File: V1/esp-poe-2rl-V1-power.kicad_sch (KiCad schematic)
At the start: 39 parts, among them Q1 WPM2015-3/TR, Q2 LMUN2211LT1G, U1 SY8089A1AAC, U2 TX4138, U6 TPS2376

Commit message: Dev
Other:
- title: ESP 16x 24VDC Input 16x 24VDC Output Module -> ESP 2x Relay Output Module with PoE
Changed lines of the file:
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@@
   (paper "A4")
   (title_block
-    (title "ESP 16x 24VDC Input 16x 24VDC Output Module")
-    (date "2023-05-05")
-    (rev "V2")
+    (title "ESP 2x Relay Output Module with PoE")
+    (date "2023-08-02")
+    (rev "V1")
   )
   (junction (at 180.34 46.99) (diameter 0) (color 0 0 0 0)

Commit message: Searching for the right connector...
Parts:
- removed U6: TPS2376, Package_SO:SOIC-8-1EP_3.9x4.9mm_P1.27mm_EP2.95x4.9mm_Mask2.71x3.4mm_ThermalVias, symbol Tales:TPS2376
- R1: value 5,6k/0,1W/0603 -> 820R/62,5mW/0402; footprint Tales:R_0603_1608Metric -> Tales:R_0402_1005Metric; Case 0603/1608 -> 0402/1005; LCSC Part # C23189 -> C423266; Mfr PN 0603WAF5601T5E -> 0402WGD8200TCE; Vendor PN C23189 -> C423266
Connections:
- net +24V: no longer R1.1
- net +5V: now also R1.1
- net GND: no longer J?.2 (Pin_2)
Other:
- note added: "5VDC"
- note added: "R_{1}"
- note added: "R_{1} = (V_{OUT} - 0,6V) * R_{2} / 0,6V V_{OUT} = (0,6 * R_{1} / R_{2}) + 0,6 V_{OUT} = (0,6 * 100k/22,1k) +0,6 V_{OUT} = 3,31V"
- note added: "R_{2}"
- note removed: "24VDC"
- note removed: "R1"
- note removed: "R2"
- note removed: "RH"
- note removed: "RL"
- note removed: "R_{H} = (V_{OUT} - 0,6V) * R_{L} / 0,6V V_{OUT} = (0,6 * R_{H} / R_{L}) + 0,6 V_{OUT} = (0,6 * 100k/22,1k) +0,6 V_{OUT} = 3,31V"
- moved on the sheet: C1, C10, C2, C3, C39, C4, C40, C5, C7, C8, D1, D2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

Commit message: Working on PoE frontend.
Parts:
- removed C4: 0,1uF/50V/0805, Tales:C_0805_2012Metric, symbol Device:C_Small
- added C23: 100nF/100V, Tales:C_1206_3216Metric, symbol Device:C_Small
- added D7: SMAJ58A, Tales:D_SMA, symbol Device:D_Zener_Small
- added R13, R14, R34: R_US, symbol Device:R_US
- added R31: 29,9k/62,5mW, Tales:R_0402_1005Metric, symbol Device:R_US
- added R32: 4,42k/62,5mW, Tales:R_0402_1005Metric, symbol Device:R_US
- added R33: 180k/62,5mW, Tales:R_0402_1005Metric, symbol Device:R_US
- added U6: TPS2376D, Package_SO:SOIC-8-1EP_3.9x4.9mm_P1.27mm_EP2.95x4.9mm_Mask2.71x3.4mm_ThermalVias, symbol Tales:TPS2376
- C1, C5: value 10uF/50V/1206 -> 10uF/50V
- C10: value 470uF/16V/10x10 -> 470uF/16V
- C2: value 47uF/35V/6,3x5,4 -> 15uF/100V; footprint Tales:CP_Elec_6.3x5.4 -> (none); Case 6,3x5,4 -> 6,3x11; LCSC Part # C263963 -> C???; Mfr Semtech -> (none); Mfr PN CK1V470MCRE54 -> (none); Vendor PN C263963 -> C???
- C3: value 22pF/50V/0603 -> 22pF/50V
- C39: value 1uF/50V/0603 -> 1uF/50V
- C40: value 0,1uF/50V/0402 -> 0,1uF/50V
- C6, C9: value 10uF/10V/0603 -> 10uF/10V
- C7: value 0,1uF/50V/0805 -> 0,1uF/50V
- C8: value 12pF/50V/0603 -> 12pF/50V
- D1: value SM4007PL/SOD-123 -> SM4007PL
- D2: value GREEN/0603 -> GREEN
- L1: value 2,2uH 1,5A -> 2,2uH/1,5A
- L2: value 33uH 2,1A -> 33uH/2,1A
- L3: value 2A 600R -> 2A/600R
- R1: value 820R/62,5mW/0402 -> 820R/62,5mW
- R131, R132: value 5k1/62,5mW/0402 -> 5k1/62,5mW
- R2: value 100k/0,125W/0805 -> 100k/0,125W
- R3: value 22,1k/0,125W/0805 -> 22,1k/0,125W
- R4: value 30mR/0,250W/0805 -> 30mR/0,250W; Technology (none) -> 1%
- R5: value 5R1/0,125W/0805 -> 5R1/0,125W; Technology (none) -> 1%
- R6: value 10k/62,5mW/0402 -> 10k/62,5mW
- R7: value 1k/62,5mW/0402 -> 1k/62,5mW
- R8: value 300k/0,125W/0805 -> 300k/0,125W; Technology (none) -> 1%
- R9: value 52,3k/0,125W/0805 -> 52,3k/0,125W; Technology (none) -> 1%
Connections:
- net +5V: now also F1.1; no longer F1.2
- net GND: now also R34.2, U6.5 (RTN)
- net at D3.1 (K): now also F1.2; no longer F1.1
- net at D1.2 (A): no longer J?.1 (Pin_1)
- net PoE+: now reaches R4.1, U2.3 (VIN)
- net PoE+: now also C2.1, C23.1, D7.1 (K), R13.1, R31.1, R34.1, U6.8 (VDD)
- net at U2.6 (EN): now also U6.6 (PG)
- net +24V: no longer names the net of D1.1 (K)
- net +24V: no longer C2.1
- new net: R13.2, R14.1, U6.7 (UVLO)
- new net: R33.1, U6.1 (ILIM)
- new net: R32.1, U6.2 (CLASS)
- new net: R31.2, U6.3 (DET)
- new net PoE-: C23.2, D7.2 (A), R14.2, R32.2, R33.2, U6.4 (VSS)
- no-connect marks 4 -> 3
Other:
- moved on the sheet: C1, C10, C2, C3, C39, C40, C5, C6, C7, C8, D1, D2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

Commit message: Development
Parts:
- removed D1: SM4007PL, Tales:D_SOD-123, symbol Device:D_Small
- removed J?: VIN, Tales:TerminalBlock_Phoenix_MKDS-3-2-5.08_1x02_P5.08mm_Horizontal, symbol Connector_Generic:Conn_01x02
- C2: footprint (none) -> Capacitor_SMD:CP_Elec_8x6.2; Case 6,3x11 -> 8x6,2; LCSC Part # C??? -> C487174; Mfr (none) -> Ymin; Mfr PN (none) -> VMMD0622A150MV; Vendor PN C??? -> C487174
- R13: value R_US -> 412k/62,5mW; footprint (none) -> Tales:R_0402_1005Metric; Case (none) -> 0402/1005; JLCPCB BOM (none) -> 1; LCSC Part # (none) -> C187991; Mfr (none) -> TA-I Tech; Mfr PN (none) -> RM04FTN4123; Technology (none) -> 1%; Vendor (none) -> JLCPCB; Vendor PN (none) -> C187991
- R14: value R_US -> 31.6k/62,5mW; footprint (none) -> Tales:R_0402_1005Metric; Case (none) -> 0402/1005; JLCPCB BOM (none) -> 1; LCSC Part # (none) -> C100371; Mfr (none) -> LIZ Elec; Mfr PN (none) -> CR0402FF3162G; Technology (none) -> 1%; Vendor (none) -> JLCPCB; Vendor PN (none) -> C100371
- R31: value 29,9k/62,5mW -> 26,7k/62,5mW; LCSC Part # C100335 -> C304992; Mfr LIZ Elec -> Ralec; Mfr PN CR0402FF2492G -> RTT022672DTH; Technology 1% -> 0,5%; Vendor PN C100335 -> C304992
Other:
- note added: "R_{2} = R_{1}/(V_{OUT} / 0,805 - 1) V_{OUT} = (R_{1} / R_{2}) + 1) * 0,805 V_{OUT} = (300k / 52,3k + 1) * 0,805 V_{OUT} = 5,42V VOLTAGE DROP AT DIODE SS34 @2A = 0,4V 5V MAIN BUS @2A = 5,02V"
- note added: "R_{CLASS}"
- note added: "R_{CLASS} = 4420R 1% CLASS 0 0.44 - 12,95W"
- note added: "R_{DET}"
- note added: "USB 2.0 -> 5V 500mA USB 3.0 -> 5V 900mA VOLTAGE DROP AT DIODE B5819W @500mA = 0,4V 5V USB BUS @500mA = 4,6V"
- note added: "VOLTAGE AT THE TAP OF THE DIVIDER R_{1}/R_{2} (PIN UVLO) MUST BE 2,5V WHEN VDD IS AT THE DESIRED TURN ON VOLTAGE. THE TOTAL RESISTANCE OF THE VOLTAGE DIVIDER WILL APPEAR IN PARALLEL WITH R_{DET} TO FORM THE EQUIVALENT RESISTANCE AT PIN DET."
- note removed: "5VDC"
- note removed: "R_{2} = R_{1}/(V_{OUT} / 0,805 - 1) V_{OUT} = (R_{1} / R_{2}) + 1) * 0,805 V_{OUT} = (300k / 52,3k + 1) * 0,805 V_{OUT} = 5,42V"
- moved on the sheet: C1, C10, C2, C23, C3, C39, C40, C5, C6, C7, C8, C9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

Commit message: Development continues!
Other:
- note added: "V_{TAP}"
- note added: "V_{TAP} MUST BE 2.5V WHEN VDD IS AT THE DESIRED TURN ON VOLTAGE. V_{TAP} = V_{DD} * R_{2} / (R_{1}+R_{2}) 2.5 = V_{DD} * 31.6 / 443.6 V_{DD} = 35.1V -> OK THE TOTAL RESISTANCE OF THE VOLTAGE DIVIDER (R_{1} + R_{2}) WILL APPEAR IN PARALLEL WITH R_{DET} TO FORM THE EQUIVALENT RESISTANCE AT PIN DET. R_{EQUIV} = (R_{1} + R_{2}) // R_{DET} R_{EQUIV} = 443.6 // 26.7 R_{EQUIV} = 25.184k -> OK"
- note removed: "VOLTAGE AT THE TAP OF THE DIVIDER R_{1}/R_{2} (PIN UVLO) MUST BE 2,5V WHEN VDD IS AT THE DESIRED TURN ON VOLTAGE. THE TOTAL RESISTANCE OF THE VOLTAGE DIVIDER WILL APPEAR IN PARALLEL WITH R_{DET} TO FORM THE EQUIVALENT RESISTANCE AT PIN DET."
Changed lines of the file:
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@@
     (effects (font (size 1.5 1.5)) (justify left bottom))
   )
-  (text "R_{CLASS} = 4420R 1%\nCLASS 0\n0.44 - 12,95W" (at 105.41 78.74 0)
+  (text "R_{CLASS} = 4420R 1%\nCLASS 0\n0.44 - 12,95W" (at 92.71 78.74 0)
     (effects (font (size 1.5 1.5)) (justify left bottom))
   )
-  (text "VOLTAGE AT THE TAP OF THE DIVIDER R_{1}/R_{2} (PIN UVLO)\nMUST BE 2,5V WHEN VDD IS AT THE DESIRED TURN ON VOLTAGE.\n\nTHE TOTAL RESISTANCE OF THE VOLTAGE DIVIDER WILL APPEAR\nIN PARALLEL WITH R_{DET} TO FORM THE EQUIVALENT RESISTANCE AT\nPIN DET."
-    (at 26.67 86.36 0)
+  (text "V_{TAP} MUST BE 2.5V WHEN VDD IS AT THE\nDESIRED TURN ON VOLTAGE.\n\nV_{TAP} = V_{DD} * R_{2} / (R_{1}+R_{2})\n2.5 = V_{DD} * 31.6 / 443.6\nV_{DD} = 35.1V -> OK\n\nTHE TOTAL RESISTANCE OF THE VOLTAGE DIVIDER\n(R_{1} + R_{2}) WILL APPEAR IN PARALLEL WITH\nR_{DET} TO FORM THE EQUIVALENT RESISTANCE AT\nPIN DET.\n\nR_{EQUIV} = (R_{1} + R_{2}) // R_{DET}\nR_{EQUIV} = 443.6 // 26.7\nR_{EQUIV} = 25.184k -> OK"
+    (at 33.02 107.95 0)
     (effects (font (size 1.5 1.5)) (justify left bottom))
   )
@@
     (effects (font (size 1.5 1.5)) (justify left bottom))
   )
+  (text "V_{TAP}" (at 59.69 49.53 0)
+    (effects (font (size 1.5 1.5)) (justify left bottom))
+  )

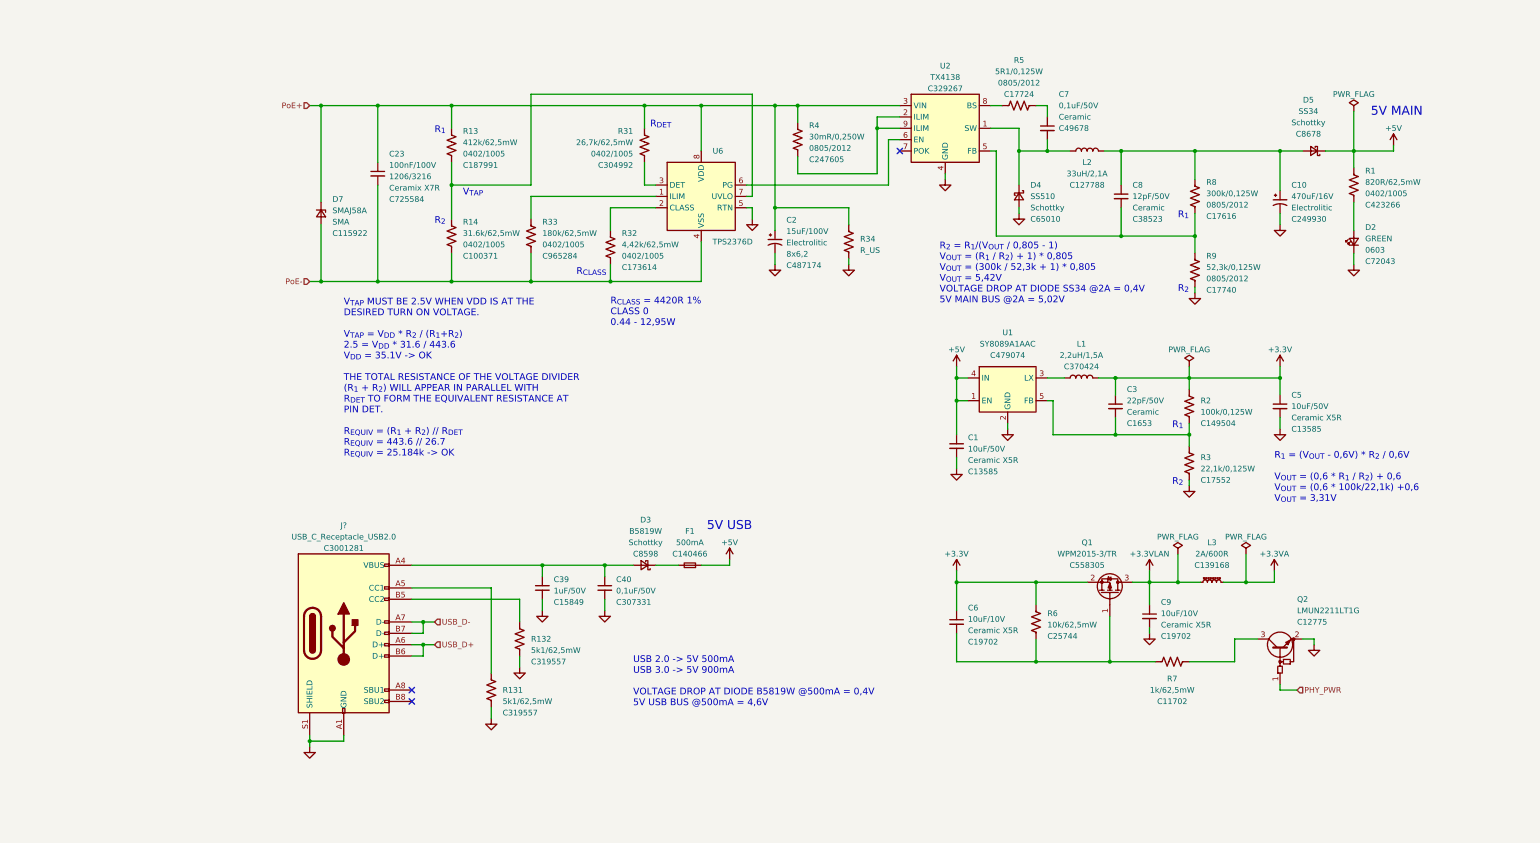
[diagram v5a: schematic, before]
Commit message: Topology ok, checking components values
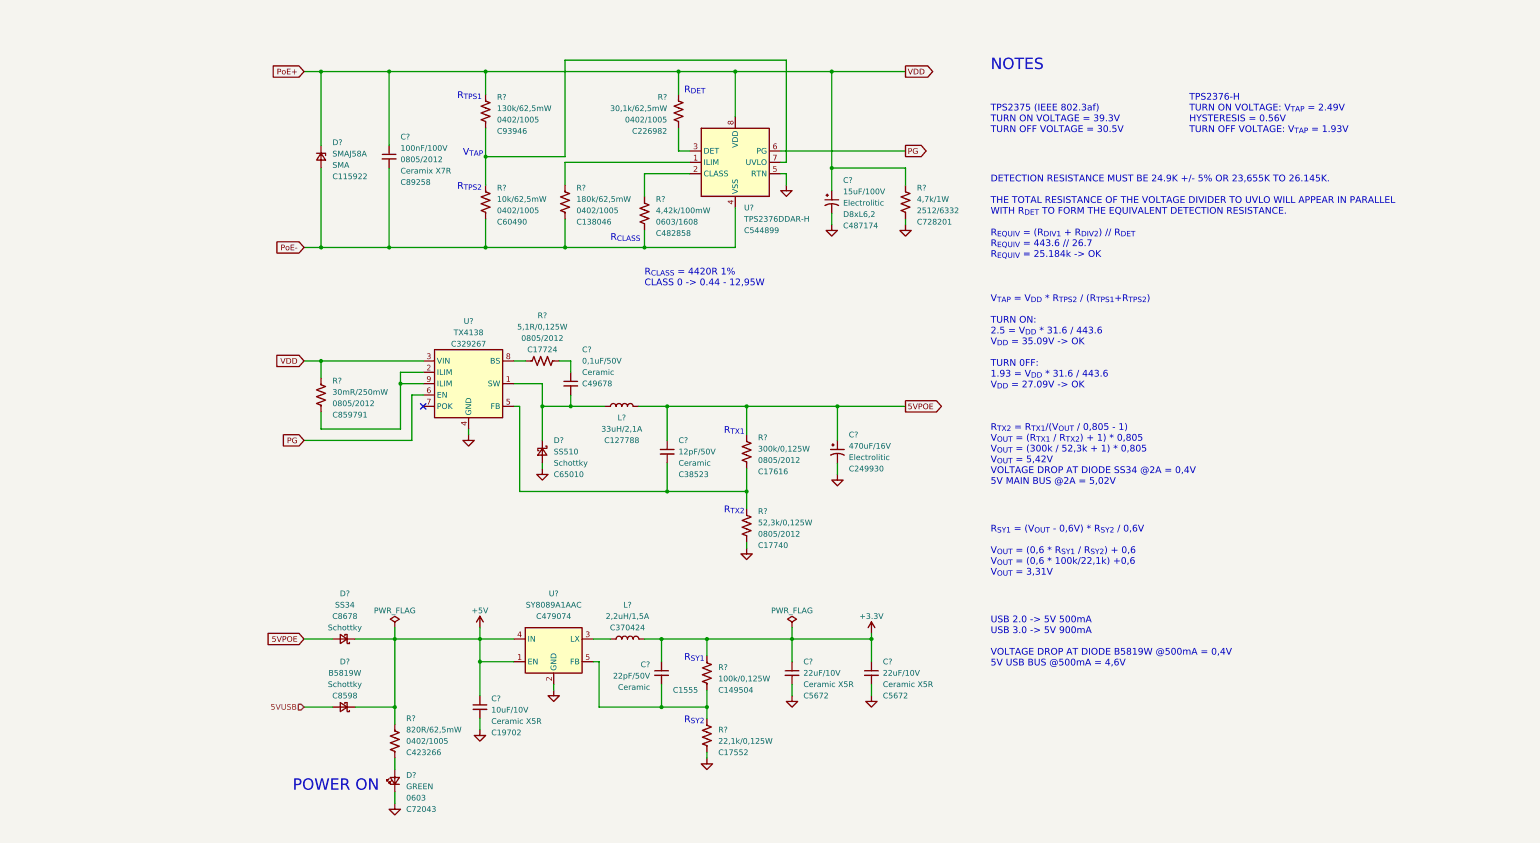
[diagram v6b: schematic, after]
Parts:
- removed C1, C5: 10uF/50V, Tales:C_1206_3216Metric, symbol Device:C_Small
- removed C10: 470uF/16V, Tales:CP_Elec_10x10, symbol Device:C_Polarized_Small_US
- removed C2: 15uF/100V, Capacitor_SMD:CP_Elec_8x6.2, symbol Device:C_Polarized_Small_US
- removed C23: 100nF/100V, Tales:C_1206_3216Metric, symbol Device:C_Small
- removed C3: 22pF/50V, Tales:C_0603_1608Metric, symbol Device:C_Small
- removed C39: 1uF/50V, Tales:C_0603_1608Metric, symbol Device:C_Small
- removed C40: 0,1uF/50V, Tales:C_0402_1005Metric, symbol Device:C_Small
- removed C6, C9: 10uF/10V, Tales:C_0603_1608Metric, symbol Device:C_Small
- removed C7: 0,1uF/50V, Tales:C_0805_2012Metric, symbol Device:C_Small
- removed C8: 12pF/50V, Tales:C_0603_1608Metric, symbol Device:C_Small
- removed D2: GREEN, Tales:LED_0603_1608Metric, symbol Device:LED_Small
- removed D3: B5819W, Tales:D_SOD-123, symbol Device:D_Schottky_Small
- removed D4: SS510, Tales:D_SMA, symbol Device:D_Schottky_Small
- removed D5: SS34, Tales:D_SMA, symbol Device:D_Schottky_Small
- removed D7: SMAJ58A, Tales:D_SMA, symbol Device:D_Zener_Small
- removed F1: 500mA, Fuse:Fuse_1206_3216Metric, symbol Device:Fuse_Small
- removed J?: USB_C_Receptacle_USB2.0, Tales:USB_C_Receptacle_JAE_DX07S024WJ1R350, symbol Connector:USB_C_Receptacle_USB2.0
- removed L1: 2,2uH/1,5A, Tales:L_3x3_H1.5, symbol Device:L
- removed L2: 33uH/2,1A, Tales:L_12x12mm_H6mm, symbol Device:L
- removed L3: 2A/600R, Inductor_SMD:L_0805_2012Metric, symbol Device:L_Ferrite_Small
- removed Q1: WPM2015-3/TR, Tales:SOT-23, symbol Device:Q_PMOS_GSD
- removed Q2: LMUN2211LT1G, Tales:SOT-23, symbol Device:Q_NPN_BEC_BRT
- removed R1: 820R/62,5mW, Tales:R_0402_1005Metric, symbol Device:R_US
- removed R13: 412k/62,5mW, Tales:R_0402_1005Metric, symbol Device:R_US
- removed R131, R132: 5k1/62,5mW, Tales:R_0402_1005Metric, symbol Device:R_US
- removed R14: 31.6k/62,5mW, Tales:R_0402_1005Metric, symbol Device:R_US
- removed R2: 100k/0,125W, Tales:R_0805_2012Metric, symbol Device:R_US
- removed R3: 22,1k/0,125W, Tales:R_0805_2012Metric, symbol Device:R_US
- removed R31: 26,7k/62,5mW, Tales:R_0402_1005Metric, symbol Device:R_US
- removed R32: 4,42k/62,5mW, Tales:R_0402_1005Metric, symbol Device:R_US
- removed R33: 180k/62,5mW, Tales:R_0402_1005Metric, symbol Device:R_US
- removed R34: R_US, symbol Device:R_US
- removed R4: 30mR/0,250W, Tales:R_0805_2012Metric, symbol Device:R_US
- removed R5: 5R1/0,125W, Tales:R_0805_2012Metric, symbol Device:R_US
- removed R6: 10k/62,5mW, Tales:R_0402_1005Metric, symbol Device:R_US
- removed R7: 1k/62,5mW, Tales:R_0402_1005Metric, symbol Device:R_US
- removed R8: 300k/0,125W, Tales:R_0805_2012Metric, symbol Device:R_US
- removed R9: 52,3k/0,125W, Tales:R_0805_2012Metric, symbol Device:R_US
- removed U1: SY8089A1AAC, Tales:TSOT-23-5, symbol Tales:SY8089AAAC
- removed U2: TX4138, Tales:SOIC-8-1EP_3.9x4.9mm_P1.27mm_EP2.29x3mm_ThermalVias, symbol Tales:TX4138
- removed U6: TPS2376D, Package_SO:SOIC-8-1EP_3.9x4.9mm_P1.27mm_EP2.95x4.9mm_Mask2.71x3.4mm_ThermalVias, symbol Tales:TPS2376
- added C? (x2): 22uF/10V, Tales:C_1206_3216Metric, symbol Device:C_Small
- added C?: 0,1uF/50V, Tales:C_0805_2012Metric, symbol Device:C_Small
- added C?: 100nF/100V, Tales:C_0805_2012Metric, symbol Device:C_Small
- added C?: 22pF/50V, Tales:C_0402_1005Metric, symbol Device:C_Small
- added C?: 15uF/100V, Capacitor_SMD:CP_Elec_8x6.2, symbol Device:C_Polarized_Small_US
- added C?: 12pF/50V, Tales:C_0603_1608Metric, symbol Device:C_Small
- added C?: 470uF/16V, Tales:CP_Elec_10x10, symbol Device:C_Polarized_Small_US
- added C?: 10uF/10V, Tales:C_0603_1608Metric, symbol Device:C_Small
- added D?: SS34, Tales:D_SMA, symbol Device:D_Schottky_Small
- added D?: SS510, Tales:D_SMA, symbol Device:D_Schottky_Small
- added D?: SMAJ58A, Tales:D_SMA, symbol Device:D_Zener_Small
- added D?: GREEN, Tales:LED_0603_1608Metric, symbol Device:LED_Small
- added D?: B5819W, Tales:D_SOD-123, symbol Device:D_Schottky_Small
- added L?: 2,2uH/1,5A, Tales:L_3x3_H1.5, symbol Device:L
- added L?: 33uH/2,1A, Tales:L_12x12mm_H6mm, symbol Device:L
- added R?: 5,1R/0,125W, Tales:R_0805_2012Metric, symbol Device:R_US
- added R?: 52,3k/0,125W, Tales:R_0805_2012Metric, symbol Device:R_US
- added R?: 130k/62,5mW, Tales:R_0402_1005Metric, symbol Device:R_US
- added R?: 4,7k/1W, Tales:R_2512_6332Metric, symbol Device:R_US
- added R?: 180k/62,5mW, Tales:R_0402_1005Metric, symbol Device:R_US
- added R?: 30,1k/62,5mW, Tales:R_0402_1005Metric, symbol Device:R_US
- added R?: 300k/0,125W, Tales:R_0805_2012Metric, symbol Device:R_US
- added R?: 100k/0,125W, Tales:R_0805_2012Metric, symbol Device:R_US
- added R?: 4,42k/100mW, Tales:R_0603_1608Metric, symbol Device:R_US
- added R?: 30mR/250mW, Tales:R_0805_2012Metric, symbol Device:R_US
- added R?: 10k/62,5mW, Tales:R_0402_1005Metric, symbol Device:R_US
- added R?: 820R/62,5mW, Tales:R_0402_1005Metric, symbol Device:R_US
- added R?: 22,1k/0,125W, Tales:R_0805_2012Metric, symbol Device:R_US
- added U?: TPS2376DDAR-H, Package_SO:SOIC-8-1EP_3.9x4.9mm_P1.27mm_EP2.95x4.9mm_Mask2.71x3.4mm_ThermalVias, symbol Tales:TPS2376
- added U?: TX4138, Tales:SOIC-8-1EP_3.9x4.9mm_P1.27mm_EP2.29x3mm_ThermalVias, symbol Tales:TX4138
- added U?: SY8089A1AAC, Tales:TSOT-23-5, symbol Tales:SY8089AAAC
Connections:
- net +3.3V: now also C?.1, C?.1, C?.1, L?.2, R?.1
- net +5V: now also C?.1, D?.1 (K), D?.1 (K), R?.1, U?.1 (EN), U?.4 (IN)
- net GND: now also C?.2, C?.2, C?.2, C?.2, C?.2, D?.1 (K), D?.2 (A), R?.2, R?.2, R?.2, U?.2 (GND), U?.4 (GND), U?.5 (RTN)
- net PoE+: now also C?.1, C?.1, D?.1 (K), R?.1, R?.1, R?.1, R?.1, U?.3 (VIN), U?.8 (VDD)
- net PoE-: now also C?.2, D?.2 (A), R?.2, R?.2, R?.2, U?.4 (VSS)
- new net: C?.1, R?.1
- new net: R?.2, U?.8 (BS)
- new net: C?.2, D?.1 (K), L?.1, U?.1 (SW)
- new net: C?.2, R?.1, R?.2, U?.5 (FB) (x2)
- new net: L?.1, U?.3 (LX)
- new net: R?.1, R?.2, U?.7 (UVLO)
- new net: R?.1, U?.1 (ILIM)
- new net: R?.1, U?.2 (CLASS)
- new net: R?.2, U?.3 (DET)
- new net: R?.2, U?.2 (ILIM), U?.9 (ILIM)
- new net: D?.2 (A), R?.2
- new net 5VPOE: C?.1, C?.1, D?.2 (A), L?.2, R?.1
- new net 5VUSB: D?.2 (A)
- new net PG: U?.6 (EN), U?.6 (PG)
- no-connect marks 3 -> 1
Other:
- note added: "DETECTION RESISTANCE MUST BE 24.9K +/- 5% OR 23,655K TO 26.145K. THE TOTAL RESISTANCE OF THE VOLTAGE DIVIDER TO UVLO WILL APPEAR IN PARALLEL WITH R_{DET} TO FORM THE EQUIVALENT DETECTION RESISTANCE. R_{EQUIV} = (R_{DIV1} + R_{DIV2}) // R_{DET} R_{EQUIV} = 443.6 // 26.7 R_{EQUIV} = 25.184k -> OK"
- note added: "NOTES"
- note added: "POWER ON"
- note added: "R_{CLASS} = 4420R 1% CLASS 0 -> 0.44 - 12,95W"
- note added: "R_{SY1}"
- note added: "R_{SY1} = (V_{OUT} - 0,6V) * R_{SY2} / 0,6V V_{OUT} = (0,6 * R_{SY1} / R_{SY2}) + 0,6 V_{OUT} = (0,6 * 100k/22,1k) +0,6 V_{OUT} = 3,31V"
- note added: "R_{SY2}"
- note added: "R_{TPS1}"
- note added: "R_{TPS2}"
- note added: "R_{TX1}"
- note added: "R_{TX2}"
- note added: "R_{TX2} = R_{TX1}/(V_{OUT} / 0,805 - 1) V_{OUT} = (R_{TX1} / R_{TX2}) + 1) * 0,805 V_{OUT} = (300k / 52,3k + 1) * 0,805 V_{OUT} = 5,42V VOLTAGE DROP AT DIODE SS34 @2A = 0,4V 5V MAIN BUS @2A = 5,02V"
- note added: "TPS2375 (IEEE 802.3af) TURN ON VOLTAGE = 39.3V TURN OFF VOLTAGE = 30.5V"
- note added: "TPS2376-H TURN ON VOLTAGE: V_{TAP} = 2.49V HYSTERESIS = 0.56V TURN OFF VOLTAGE: V_{TAP} = 1.93V"
- note added: "V_{TAP} = V_{DD} * R_{TPS2} / (R_{TPS1}+R_{TPS2}) TURN ON: 2.5 = V_{DD} * 31.6 / 443.6 V_{DD} = 35.09V -> OK TURN 0FF: 1.93 = V_{DD} * 31.6 / 443.6 V_{DD} = 27.09V -> OK"
- note removed: "5V MAIN"
- note removed: "5V USB"
- note removed: "R_{1}"
- note removed: "R_{1} = (V_{OUT} - 0,6V) * R_{2} / 0,6V V_{OUT} = (0,6 * R_{1} / R_{2}) + 0,6 V_{OUT} = (0,6 * 100k/22,1k) +0,6 V_{OUT} = 3,31V"
- note removed: "R_{2}"
- note removed: "R_{2} = R_{1}/(V_{OUT} / 0,805 - 1) V_{OUT} = (R_{1} / R_{2}) + 1) * 0,805 V_{OUT} = (300k / 52,3k + 1) * 0,805 V_{OUT} = 5,42V VOLTAGE DROP AT DIODE SS34 @2A = 0,4V 5V MAIN BUS @2A = 5,02V"
- note removed: "R_{CLASS} = 4420R 1% CLASS 0 0.44 - 12,95W"
- note removed: "V_{TAP} MUST BE 2.5V WHEN VDD IS AT THE DESIRED TURN ON VOLTAGE. V_{TAP} = V_{DD} * R_{2} / (R_{1}+R_{2}) 2.5 = V_{DD} * 31.6 / 443.6 V_{DD} = 35.1V -> OK THE TOTAL RESISTANCE OF THE VOLTAGE DIVIDER (R_{1} + R_{2}) WILL APPEAR IN PARALLEL WITH R_{DET} TO FORM THE EQUIVALENT RESISTANCE AT PIN DET. R_{EQUIV} = (R_{1} + R_{2}) // R_{DET} R_{EQUIV} = 443.6 // 26.7 R_{EQUIV} = 25.184k -> OK"
- title: ESP 2x Relay Output Module with PoE -> (none)
